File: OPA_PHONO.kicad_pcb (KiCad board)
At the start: 4 copper layers, 99 x 55 mm, 62 parts, among them J1 Barrel_Jack, J2 Conn_Coaxial_x2, J3 Conn_Coaxial_x2, U1 OPA1644AxD, U2 OPA1612AxD, U3 LT3032-12

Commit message: CHANGE POWER SUPPLY
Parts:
- removed C26: 2200uF, Capacitor_SMD:CP_Elec_18x17.5
- removed C27, C28: 1u, Capacitor_SMD:C_0402_1005Metric
- removed D1, D2: US1D, Diode_SMD:D_SMA
- removed J1: Barrel_Jack, Connector_BarrelJack:BarrelJack_CUI_PJ-063AH_Horizontal
- added J4: USB_C_Receptacle_USB2.0, Connector_USB:USB_C_Receptacle_JAE_DX07S016JA1R1500, F.Cu at (199.2, 79.8)
- added R27: 120k, Resistor_SMD:R_0402_1005Metric, F.Cu at (194.3, 91.2)
- added R28: 470k, Resistor_SMD:R_0402_1005Metric, F.Cu at (195.3, 92.2)
- C14: value 10u -> 1u; footprint Capacitor_SMD:C_0805_2012Metric -> Capacitor_SMD:C_0402_1005Metric
- C15: value 10n -> 10u; footprint Capacitor_SMD:C_0402_1005Metric -> Capacitor_SMD:C_0805_2012Metric
- C16: value 10n -> 1u
- C17, C18: value 10u -> 100n; footprint Capacitor_SMD:C_0805_2012Metric -> Capacitor_SMD:C_0402_1005Metric
- C23, C24, C25: value 2200uF -> 10u; footprint Capacitor_SMD:CP_Elec_18x17.5 -> Capacitor_SMD:C_0805_2012Metric
- R16, R4: value 10k -> 16k
- R20, R8: value 100R -> 300R
- R25: value 4.7R -> 470k; footprint Resistor_SMD:R_2512_6332Metric -> Resistor_SMD:R_0402_1005Metric
- R26: value 4.7R -> ?; footprint Resistor_SMD:R_2512_6332Metric -> Resistor_SMD:R_0402_1005Metric
- U3: value LT3032-12 -> LTC3265xDHC; footprint Package_DFN_QFN:Linear_DE14MA -> Package_DFN_QFN:DFN-18-1EP_3x5mm_P0.5mm_EP1.66x4.4mm
- moved C16 67.5 mm to (196.8, 89.2), turned to 90 degrees
- moved U3 66.3 mm to (199.3, 91.2), turned to 0 degrees
- moved C14 66.0 mm to (199.3, 94.7)
- moved C17 65.6 mm to (202.8, 90.7), turned to 180 degrees
- moved C25 64.9 mm to (194.8, 93.7), turned to 180 degrees
- moved C15 62.5 mm to (198.8, 96.2), turned to 180 degrees
- moved C13 62.0 mm to (194.3, 89.7), turned to 0 degrees
- moved C18 58.6 mm to (196.3, 91.2), turned to 180 degrees
- moved C23 41.0 mm to (202.3, 87.2)
- moved C24 31.6 mm to (204.3, 87.2), turned to -90 degrees
- moved R25 15.9 mm to (203.8, 89.7), turned to 0 degrees
- moved R26 6.67 mm to (204.8, 90.7), turned to 0 degrees
- moved C6 2.25 mm to (171.8, 96.7)
- moved C12 2.25 mm to (171.8, 98.2)
- moved R24 2.24 mm to (171.8, 100.2)
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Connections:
- net /LEFT/IN2 renamed /LEFT/RIAA
- net /LEFT/IN2_R renamed /LEFT/RIAA_R
- net /LEFT/IN2_RC renamed /LEFT/RIAA_RC
- net /RIGHT/IN2 renamed /RIGHT/RIAA
- net /RIGHT/IN2_R renamed /RIGHT/RIAA_R
- net /RIGHT/IN2_RC renamed /RIGHT/RIAA_RC
- C13 pad 2: /POWER/REG_P_R -> /POWER/VIN
- C14 pad 1: /POWER/REN_N_R -> /POWER/CINVN
- C14 pad 2: GND -> /POWER/CINVP
- C15 pad 1: /POWER/BYPP -> GND
- C15 pad 2: +12V -> /POWER/VOUTN
- C16 pad 1: -12V -> /POWER/CBSTP
- C16 pad 2: /POWER/BYPN -> /POWER/CBSTN
- C17 pad 2: +12V -> /POWER/BYPP
- C18 pad 1: -12V -> /POWER/BYPN
- C23 pad 1: /POWER/REG_P -> GND
- C23 pad 2: GND -> /POWER/VOUTP
- C24 pad 2: /POWER/REG_N -> +12V
- C25 pad 1: /POWER/REG_P_R -> -12V
- R25 pad 1: /POWER/REG_P -> +12V
- R25 pad 2: /POWER/REG_P_R -> /POWER/ADJP
- R26 pad 1: /POWER/REG_N -> /POWER/ADJP
- R26 pad 2: /POWER/REN_N_R -> GND
- U3 pad 1: +12V -> /POWER/CBSTN
- U3 pad 10: /POWER/REN_N_R -> /POWER/CINVP
- U3 pad 11: /POWER/BYPN -> /POWER/VOUTP
- U3 pad 12: /POWER/REG_P_R -> GND
- U3 pad 13: unconnected-(U3-Pad13) -> /POWER/VIN
- U3 pad 14: /POWER/REG_P_R -> GND
- U3 pad 2: unconnected-(U3-Pad2) -> /POWER/CBSTP
- U3 pad 3: /POWER/BYPP -> /POWER/VIN
- U3 pad 4: GND -> /POWER/VIN
- U3 pad 5: GND -> /POWER/BYPN
- U3 pad 6: /POWER/REN_N_R -> /POWER/ADJN
- U3 pad 8: unconnected-(U3-Pad8) -> /POWER/VOUTN
- U3 pad 9: /POWER/REN_N_R -> /POWER/CINVN
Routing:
- net GND: track 148.5 -> 21.9 mm, vias 114 -> 52
- net /POWER/REG_P_R: track 108.3 -> 0.00 mm, vias 12 -> 0
- net /POWER/REN_N_R: track 99.8 -> 0.00 mm, vias 8 -> 0
- net /POWER/REG_P: track 50.9 -> 0.00 mm, vias 5 -> 0
- net /POWER/REG_N: track 44.5 -> 0.00 mm, vias 5 -> 0
- net /RIGHT/OUT_RC: track 27.3 -> 3.74 mm, vias 4 -> 3
- net /POWER/AC_A: track 12.7 -> 0.00 mm
- net -12V: track 14.1 -> 6.31 mm, vias 4 -> 2
- net +12V: track 14.5 -> 6.73 mm, vias 4 -> 2
- net /OUT_R: track 24.9 -> 19.1 mm
- net /RIGHT/OUT2: track 6.11 -> 3.08 mm
- net /LEFT/OUT_RC: track 26.2 -> 23.6 mm, vias 3 -> 1
- net /POWER/BYPN: track 1.81 -> 0.00 mm, vias 1 -> 0
- net /POWER/BYPP: track 1.61 -> 0.00 mm
- removed copper zone on F.Cu, net /POWER/REG_P_R
- removed copper zone on F.Cu, net /POWER/REN_N_R
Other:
- board size 99 x 55 mm -> 99 x 30 mm

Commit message: update layout
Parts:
- removed J3: Conn_Coaxial_x2, OPA_PHONO:PJRAS2X1S01X
- added C26: 4.7u, Capacitor_SMD:C_0402_1005Metric, F.Cu at (196.3, 83.7)
- added C27: 4.7u, Capacitor_SMD:C_0402_1005Metric, F.Cu at (195.3, 85.7)
- added C28: 4.7u, Capacitor_SMD:C_0402_1005Metric, F.Cu at (189.8, 77.2)
- added C29: 4.7u, Capacitor_SMD:C_0402_1005Metric, F.Cu at (196.3, 85.7)
- added C30: 4.7u, Capacitor_SMD:C_0402_1005Metric, F.Cu at (189.8, 78.2)
- added Je: Conn_Coaxial_x2, OPA_PHONO:PJRAS2X1S01X, B.Cu at (168.3, 85.2)
- C13, C15, C23, C24, C25: value 10u -> 4.7u; footprint Capacitor_SMD:C_0805_2012Metric -> Capacitor_SMD:C_0402_1005Metric
- J2: moved to B.Cu
- J4: value USB_C_Receptacle_USB2.0 -> UJC-HP-3-SMT-TR; footprint Connector_USB:USB_C_Receptacle_JAE_DX07S016JA1R1500 -> Connector_USB:USB_C_Receptacle_Palconn_UTC16-G; moved to B.Cu
- moved R15 28.7 mm to (129.3, 87.2), turned to 0 degrees
- moved R14 28.6 mm to (129.8, 88.7), turned to 90 degrees
- moved C19 28.2 mm to (129.3, 85.2), turned to 0 degrees
- moved R22 27.9 mm to (129.3, 83.2), turned to 0 degrees
- moved C11 27.2 mm to (129.8, 81.7), turned to -90 degrees
- moved R18 23.4 mm to (148.3, 84.7), turned to 90 degrees
- moved C7 22.1 mm to (127.8, 86.7), turned to 90 degrees
- moved C9 21.9 mm to (145.3, 87.2), turned to 180 degrees
- moved C3 21.9 mm to (145.4, 82.2), turned to 180 degrees
- moved C2 21.6 mm to (145.3, 79.7), turned to 180 degrees
- moved C8 21.5 mm to (145.3, 84.7), turned to 180 degrees
- moved U1 21.2 mm to (134.3, 85.2), turned to 0 degrees
- moved C10 20.4 mm to (162.3, 79.7)
- moved R13 20.3 mm to (129.3, 86.2), turned to 0 degrees
- moved R17 20.3 mm to (148.3, 86.7), turned to -90 degrees
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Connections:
- net /LEFT/FB3 renamed /LEFT/FBTRIM
- net /LEFT/OUT3 renamed /LEFT/TRIM
- net /RIGHT/FB3 renamed /RIGHT/FBTRIM
- net /RIGHT/OUT3 renamed /RIGHT/TRIM
- C23 pad 2: /POWER/VOUTP -> /POWER/VIN
- C24 pad 2: +12V -> /POWER/VOUTN
- C25 pad 1: -12V -> GND
- C25 pad 2: GND -> /POWER/VOUTP
- J2 pad 1: /IN_R -> (no net)
- J2 pad 2: /IN_L -> (no net)
- J2 pad S1: (no net) -> GND
- J2 pad S2: (no net) -> GND
- J2 pad T1: (no net) -> /IN_L
- J2 pad T2: (no net) -> /IN_R
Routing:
- net /IN_L: track 40.5 -> 12.9 mm, vias 0 -> 1
- net /OUT_L: track 30.2 -> 3.11 mm, vias 1 -> 0
- net /RIGHT/OUT1: track 4.26 -> 28.1 mm
- net GND: track 21.9 -> 0.00 mm, vias 52 -> 16
- net /LEFT/OUT_RC: track 23.6 -> 3.62 mm, vias 1 -> 2
- net /RIGHT/TRIM: track 23.0 -> 3.12 mm, vias 0 -> 1
- net /LEFT/TRIM: track 21.7 -> 4.66 mm, vias 0 -> 1
- net /OUT_R: track 19.1 -> 3.60 mm
- net /LEFT/OUT1: track 3.99 -> 19.2 mm
- net /LEFT/RIAA: track 10.9 -> 24.8 mm
- net /IN_R: track 25.3 -> 12.1 mm, vias 0 -> 1
- net /RIGHT/RIAA: track 14.4 -> 23.3 mm
- net +12V: track 6.73 -> 0.00 mm, vias 2 -> 0
- net -12V: track 6.31 -> 0.00 mm, vias 2 -> 0
- net /LEFT/RIAA_RC: track 4.24 -> 0.00 mm
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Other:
- board size 99 x 30 mm -> 99 x 15 mm

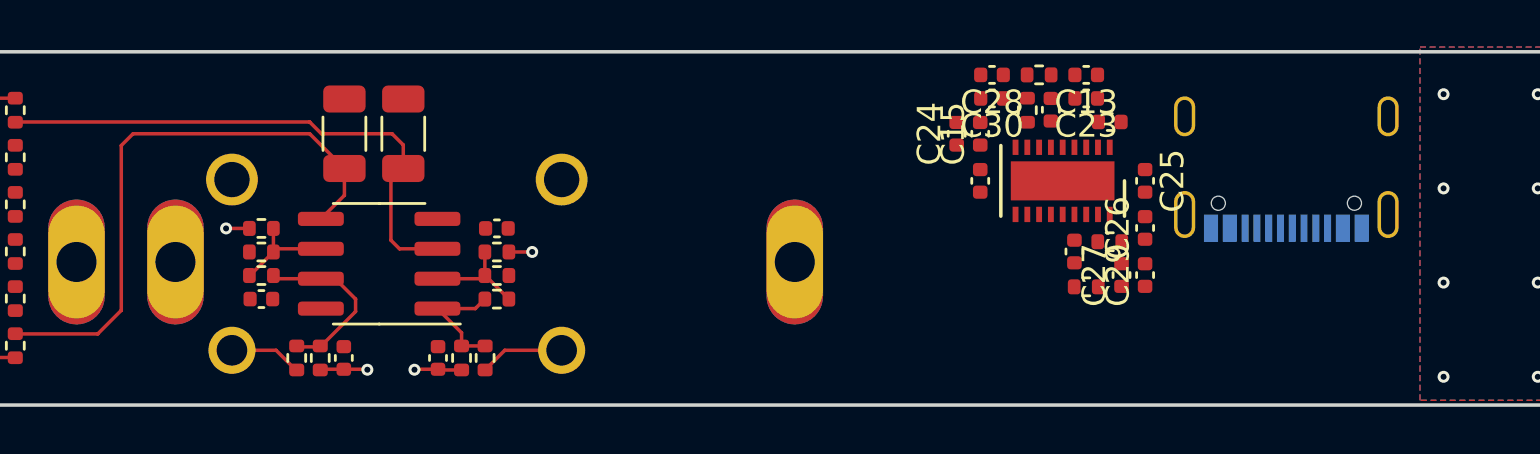
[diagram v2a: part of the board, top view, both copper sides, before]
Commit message: add usb c connector
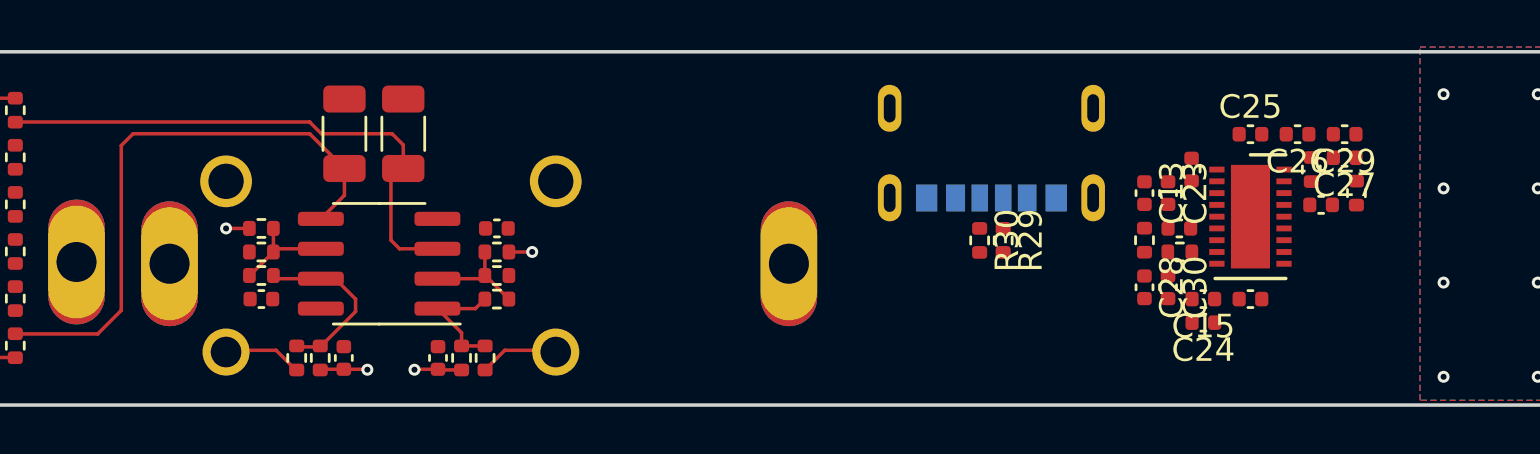
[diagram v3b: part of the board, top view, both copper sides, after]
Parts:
- removed J4: UJC-HP-3-SMT-TR, Connector_USB:USB_C_Receptacle_Palconn_UTC16-G
- removed Je: Conn_Coaxial_x2, OPA_PHONO:PJRAS2X1S01X
- added J1: PJRAS2X1S01X, OPA_PHONO:PJRAS2X1S01X, B.Cu at (168.1, 85.3)
- added J3: UJC-HP-3-SMT-TR, OPA_PHONO:CUI_UJC-HP-3-SMT-TR, B.Cu at (189.8, 82.4)
- added R29: 5.1k, Resistor_SMD:R_0402_1005Metric, F.Cu at (190.3, 84.2)
- added R30: 5.1k, Resistor_SMD:R_0402_1005Metric, F.Cu at (189.3, 84.2)
- J2: value Conn_Coaxial_x2 -> PJRAS2X1S01X
- R26: value ? -> 120k
- moved C24 13.2 mm to (198.8, 87.7), turned to 180 degrees
- moved C14 12.5 mm to (200.8, 86.7), turned to 0 degrees
- moved R26 12.1 mm to (205.3, 82.2), turned to -90 degrees
- moved C15 11.8 mm to (198.8, 86.7), turned to 180 degrees
- moved C28 11.1 mm to (196.3, 86.2), turned to -90 degrees
- moved C30 11.0 mm to (197.3, 86.2), turned to -90 degrees
- moved C27 10.7 mm to (204.8, 80.7), turned to 180 degrees
- moved C17 10.7 mm to (203.8, 82.7), turned to 180 degrees
- moved C29 10.4 mm to (204.8, 79.7), turned to 180 degrees
- moved R25 9.09 mm to (203.4, 81.2), turned to -90 degrees
- moved R28 8.84 mm to (197.8, 84.7), turned to 180 degrees
- moved R27 8.33 mm to (196.3, 84.2), turned to -90 degrees
- moved U3 8.12 mm to (200.8, 83.2), turned to 0 degrees
- moved C26 7.60 mm to (202.8, 79.7), turned to 180 degrees
- moved C18 7.43 mm to (197.8, 83.7), turned to 180 degrees
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
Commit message: Update component fields
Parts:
- C19, C20, C21, C22: value 1u -> 4.7u
- C2, C3, C8, C9: footprint Capacitor_SMD:C_1206_3216Metric -> Capacitor_SMD:C_1210_3225Metric
- R1, R13: value R_US -> 47k
- moved C9 1.52 mm to (145.3, 88.7)
- moved C2 1.48 mm to (145.3, 78.2)
- moved C8 0.50 mm to (145.3, 85.2)
- moved C3 0.48 mm to (145.4, 81.7)

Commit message: routed all nets
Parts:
- removed C15, C25, C29, C30: 4.7u, Capacitor_SMD:C_0402_1005Metric
- C1, C7: value C -> NP
- C11, C12, C5, C6: value 470n -> 1u
- C13, C19, C20, C21, C22: value 4.7u -> 1u
- C17, C18: value 100n -> 1u
- C23, C24, C26, C27, C28: value 4.7u -> 10u; footprint Capacitor_SMD:C_0402_1005Metric -> Capacitor_SMD:C_0805_2012Metric
- moved C3 33.0 mm to (178.3, 79.7), turned to 90 degrees
- moved C2 29.6 mm to (174.8, 79.7), turned to 90 degrees
- moved R6 21.3 mm to (169.3, 79.2)
- moved R5 20.0 mm to (168.3, 79.2), turned to -90 degrees
- moved R4 19.0 mm to (167.3, 79.2)
- moved R16 15.3 mm to (160.3, 79.2), turned to 90 degrees
- moved R17 13.3 mm to (159.3, 79.2)
- moved C9 11.7 mm to (152.8, 79.7), turned to 90 degrees
- moved R18 11.4 mm to (158.3, 79.2), turned to -90 degrees
- moved C13 8.94 mm to (204.3, 86.2), turned to 180 degrees
- moved C8 6.79 mm to (149.3, 79.7), turned to 90 degrees
- moved R29 4.51 mm to (190.3, 79.7), turned to 90 degrees
- moved R30 4.51 mm to (189.3, 79.7), turned to 90 degrees
- moved C26 3.04 mm to (199.8, 80.2), turned to 0 degrees
- moved C24 2.69 mm to (196.3, 88.7), turned to 0 degrees
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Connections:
- C13 pad 2: /POWER/VIN -> /POWER/VOUTP
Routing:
- net GND: track 0.00 -> 57.2 mm, vias 16 -> 53
- net /RIGHT/TRIM: track 3.12 -> 38.9 mm, vias 1 -> 2
- net /RIGHT/OUT_RC: track 3.57 -> 37.1 mm
- net /LEFT/OUT_RC: track 3.62 -> 36.3 mm
- net /POWER/VIN: track 0.00 -> 30.1 mm, vias 0 -> 4
- net /LEFT/TRIM: track 4.66 -> 33.5 mm, vias 1 -> 2
- net /LEFT/OUT1: track 19.2 -> 43.2 mm, vias 0 -> 2
- net /RIGHT/OUT1: track 28.1 -> 48.9 mm, vias 0 -> 2
- net /LEFT/RIAA: track 24.8 -> 6.72 mm
- net /RIGHT/RIAA: track 23.3 -> 9.00 mm
- net -12V: track 0.00 -> 11.9 mm, vias 0 -> 4
- net /POWER/VOUTP: track 0.00 -> 11.1 mm, vias 0 -> 2
- net +12V: track 0.00 -> 10.1 mm, vias 0 -> 4
- net /RIGHT/RIAA_RC: track 0.00 -> 9.61 mm
- net /LEFT/RIAA_RC: track 0.00 -> 9.61 mm
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
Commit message: Clean DRC
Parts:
- moved J1 38.0 mm to (153.2, 50.2), turned to 0 degrees
- moved J2 37.9 mm to (123.2, 50.2), turned to 0 degrees
- moved C24 37.2 mm to (180.5, 55.0), turned to -90 degrees
- moved C28 35.7 mm to (182.5, 53.0), turned to 90 degrees
- moved C14 35.3 mm to (181.0, 59.0), turned to -90 degrees
- moved R27 32.9 mm to (184.0, 54.5), turned to -90 degrees
- moved R28 32.8 mm to (183.5, 56.0), turned to 180 degrees
- moved C18 32.5 mm to (185.0, 53.5), turned to 90 degrees
- moved C13 31.9 mm to (183.0, 62.5), turned to 90 degrees
- moved J3 30.9 mm to (173.5, 56.2)
- moved R29 30.9 mm to (174.0, 53.5)
- moved R30 30.9 mm to (173.0, 53.5)
- moved R4 30.6 mm to (151.5, 53.0), turned to 180 degrees
- moved U3 30.4 mm to (184.5, 59.0), turned to -90 degrees
- moved C1 30.1 mm to (126.0, 60.5)
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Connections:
- J3 pad S1: unconnected-(J3-Pad24) -> unconnected-(J3-PadS1)
- J3 pad S2: unconnected-(J3-Pad24) -> unconnected-(J3-PadS2)
- J3 pad S3: unconnected-(J3-Pad24) -> unconnected-(J3-PadS3)
- J3 pad S4: (no net) -> unconnected-(J3-PadS4)
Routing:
- net /POWER/VIN: track 30.1 -> 3.93 mm
- net GND: track 57.2 -> 81.0 mm
- net /LEFT/TRIM: track 33.5 -> 37.0 mm
- net /LEFT/OUT1: track 43.2 -> 45.3 mm
- net /RIGHT/OUT_RC: track 37.1 -> 39.1 mm
- net /RIGHT/RIAA_RC: track 9.61 -> 7.69 mm
- net /LEFT/RIAA_RC: track 9.61 -> 7.69 mm
- net /RIGHT/OUT1: track 48.9 -> 47.0 mm
- net /LEFT/OUT_RC: track 36.3 -> 37.9 mm
- net /POWER/VOUTP: track 11.1 -> 12.5 mm, vias 2 -> 3
- net /POWER/VOUTN: track 4.89 -> 3.52 mm
- net /POWER/BYPN: track 5.03 -> 3.76 mm
- net /RIGHT/FBTRIM: track 3.28 -> 4.51 mm
- net /LEFT/FB1: track 3.18 -> 4.40 mm
- net /OUT_L: track 3.11 -> 4.02 mm
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- added copper zone on F.Cu, net +12V
- added copper zone on F.Cu, net -12V
- added copper zone on B.Cu, net /POWER/VIN
- added copper zone on F.Cu, net /POWER/VIN
- added copper zone on F.Cu, net /POWER/VOUTN
- added copper zone on F.Cu, net /POWER/VOUTP
- removed copper zone on In2.Cu, net GND
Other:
- board size 99 x 15 mm -> 100 x 15 mm
- rule pad_to_mask_clearance: 0 -> 0.0762

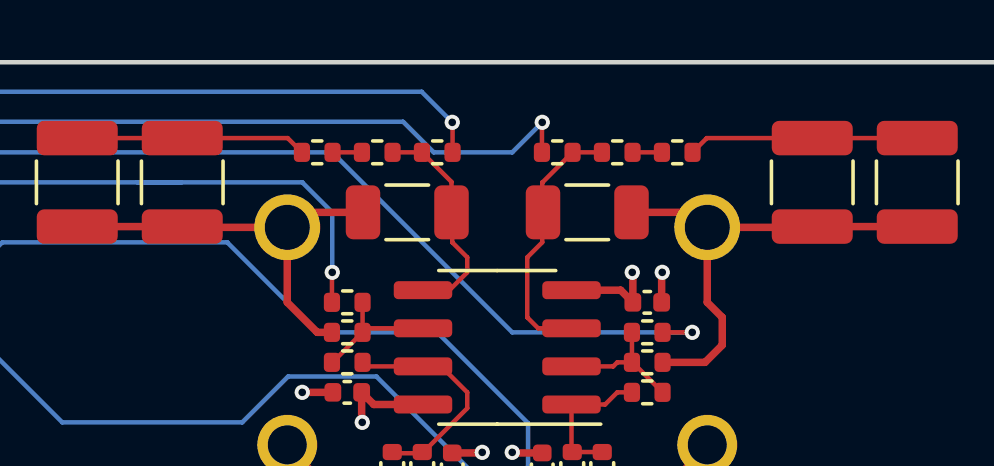
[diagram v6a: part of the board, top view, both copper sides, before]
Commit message: simplify BOM
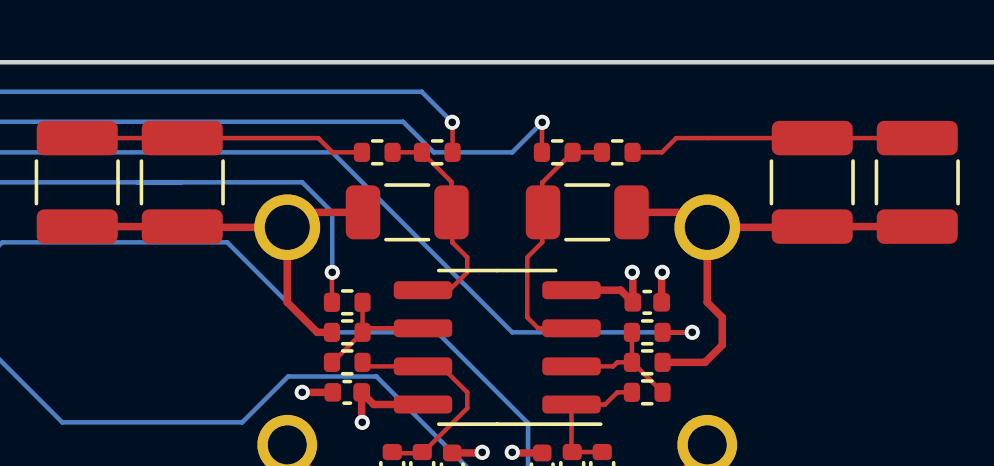
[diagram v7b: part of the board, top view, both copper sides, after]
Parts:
- removed R18: 127R, Resistor_SMD:R_0402_1005Metric
- removed R20: 300R, Resistor_SMD:R_0402_1005Metric
- R10, R11, R22, R23: value 470k -> 47k
- R17, R5: value 2.2k -> 2.32k
- R21, R9: value 27.4k -> 47k
- R25, R28: value 470k -> 20.5k
- R26, R27: value 120k -> 5.1k
- R6: value 127R -> 100R
- R8: value 300R -> 100R
- moved R6 12.5 mm to (144.5, 59.0)
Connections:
- net +12V renamed /POWER/+6V
- net -12V renamed /POWER/-6V
- R17 pad 1: /LEFT/RIAA_R -> /LEFT/RIAA_RC
- R5 pad 1: /RIGHT/RIAA_R -> /RIGHT/RIAA_RC
- R6 pad 1: /RIGHT/RIAA_R -> GND
- R6 pad 2: /RIGHT/RIAA_RC -> /LEFT/FB2
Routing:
- net /RIGHT/RIAA_RC: track 7.69 -> 9.69 mm
- net /LEFT/RIAA_RC: track 7.69 -> 9.69 mm
- net /RIGHT/RIAA_R: track 0.98 -> 0.00 mm
- net /LEFT/RIAA_R: track 0.98 -> 0.00 mm

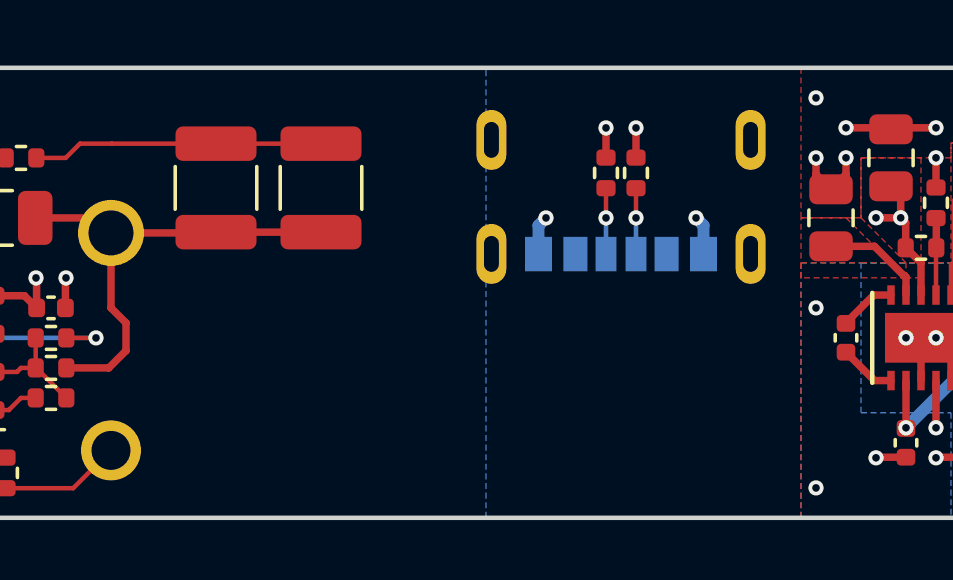
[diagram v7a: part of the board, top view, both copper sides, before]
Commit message: Add graphics, simplify output resistor
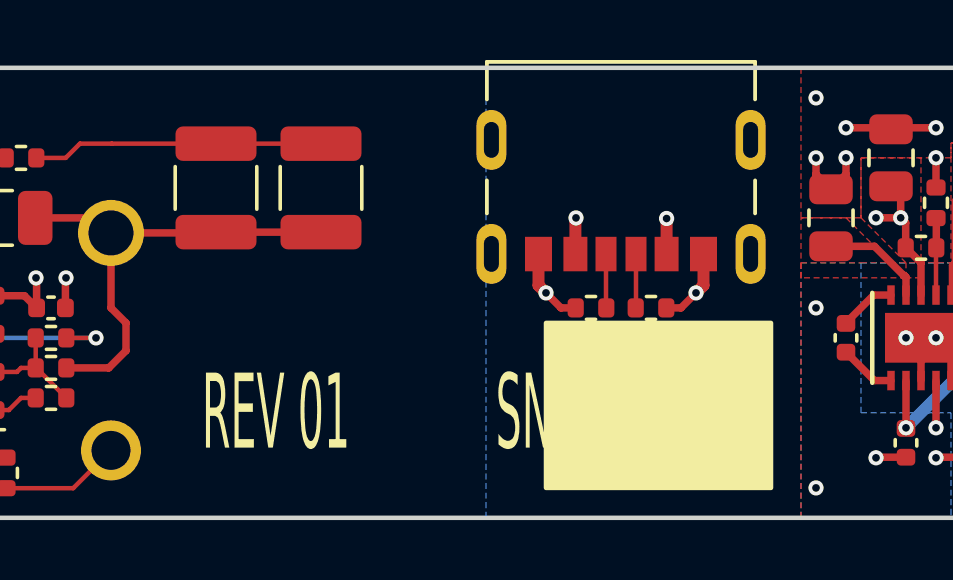
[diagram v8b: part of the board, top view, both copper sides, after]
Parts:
- added G***: LOGO, LOGO, B.Cu at (187.5, 57.5)
- added Ge: LOGO, LOGO, B.Cu at (180.5, 99.5)
- J3: moved to F.Cu
- R12, R15, R24, R3, R6, R8: value 100R -> 68R
- R14, R19, R2, R7: value 3.3k -> 2.32k
- moved R29 4.74 mm to (172.5, 58.0), turned to 180 degrees
- moved R30 4.74 mm to (174.5, 58.0), turned to 0 degrees
- turned J3 to 180 degrees
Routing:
- net /POWER/VIN: track 3.93 -> 6.33 mm, vias 4 -> 6
- net GND: track 81.0 -> 81.6 mm, vias 53 -> 51
- net /CC2: track 2.20 -> 1.80 mm, vias 1 -> 0
- net /CC1: track 2.20 -> 1.80 mm, vias 1 -> 0
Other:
- board text added: "OPA_PHONO"
- board text added: "REV 01"
- board text added: "SN:"
